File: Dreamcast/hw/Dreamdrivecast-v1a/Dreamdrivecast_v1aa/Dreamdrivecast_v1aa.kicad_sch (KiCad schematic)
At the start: 73 parts, among them CN1 Molex_52602_0579, J1 USB_C_Receptacle_USB2.0, J2 Micro_SD_Card, J3 POWER, J4 Dreamcast Data, J6 Dreamcast Control Lines, J7 MCU Databus, J8 Dreamcast Misc, J9 MCU Misc, SW1 Lid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

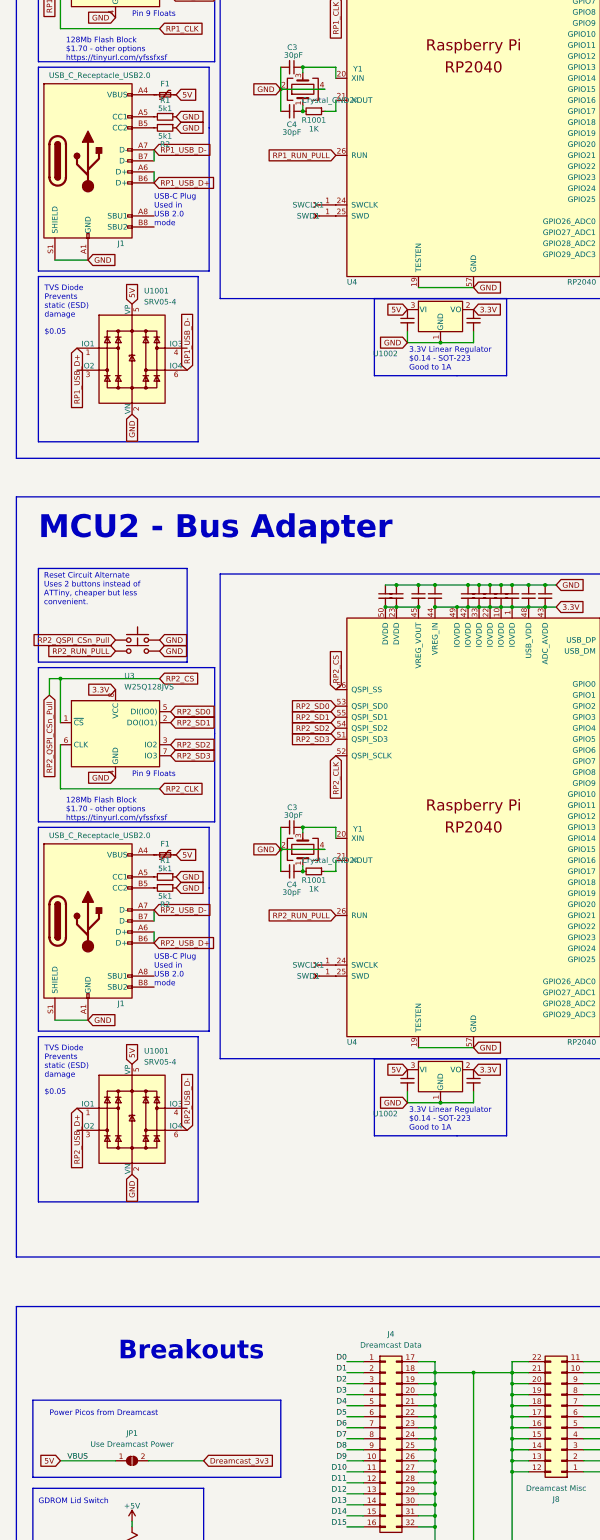
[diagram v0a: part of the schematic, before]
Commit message: Update pcb and schematic to reflect diode and removal of second mosfet connected to mcu2
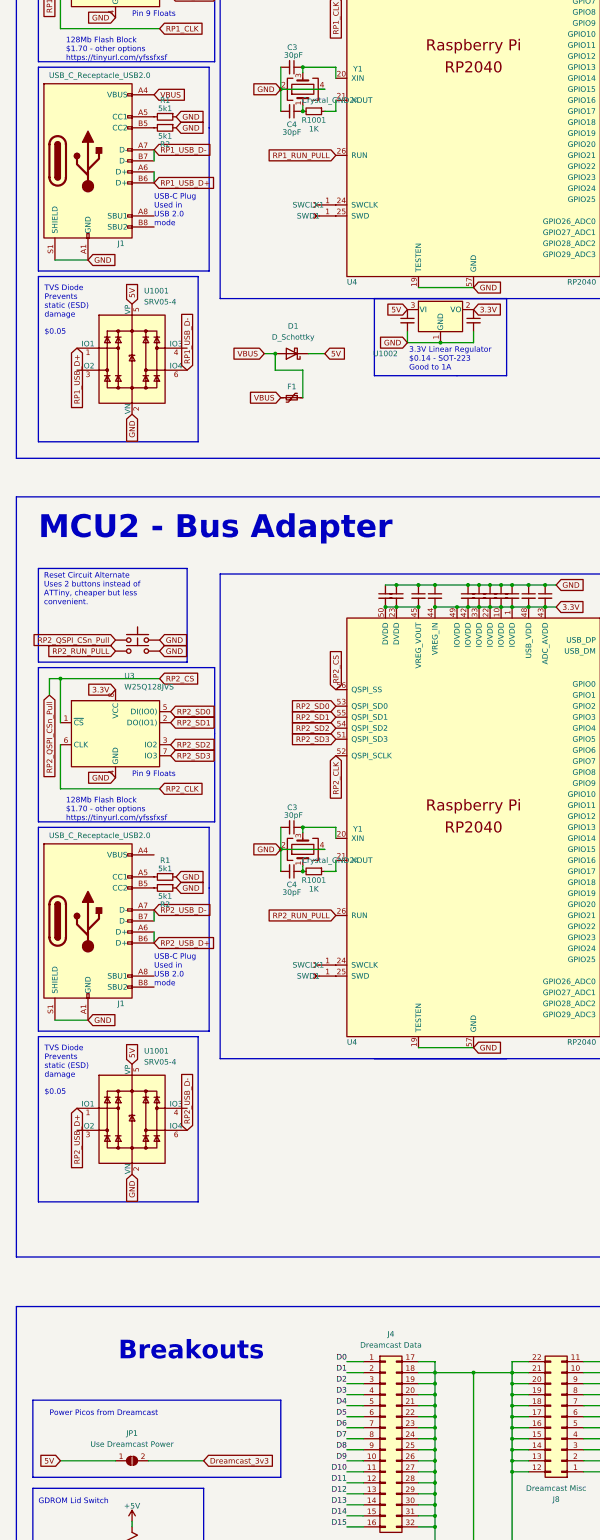
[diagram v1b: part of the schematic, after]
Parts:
- removed C1001, C1002: 1uF, Capacitor_SMD:C_0402_1005Metric, symbol Device:C_Small
- removed F1 (x2): 1.1A, Fuse:Fuse_1206_3216Metric, symbol Device:Polyfuse_Small
- removed U1002: AMS1117-3.3, Package_TO_SOT_SMD:SOT-223, symbol Regulator_Linear:AZ1117-3.3
- added D1: D_Schottky, Diode_SMD:D_SOD-123F, symbol Device:D_Schottky
- added F1: 1.1A, Fuse:Fuse_1206_3216Metric, symbol Device:Polyfuse_Small
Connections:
- net 5V: now also D1.1 (K)
- net VBUS: now reaches J1.A4 (VBUS), J1.A9 (VBUS), J1.B4 (VBUS), J1.B9 (VBUS)
- net VBUS: now also D1.2 (A), F1.1, F1.2
